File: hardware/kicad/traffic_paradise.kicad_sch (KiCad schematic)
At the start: 48 parts, among them J2 USB C, Q1 SS8050, Q2 SS8050, SW1 SW_Push, SW2 SW_Push, SW3 SW_Push, U1 ESP32-WROOM-32, U2 AMS1117-3.3, U3 USBLC6-2SC6, U4 CP2102N-A02-GQFN28

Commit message: Update KiCAD files
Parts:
- added R20, R21: 2k, Resistor_SMD:R_0402_1005Metric, symbol Device:R_Small_US
- D1: footprint Diode_SMD:D_0805_2012Metric -> Diode_SMD:D_SMA
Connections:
- net +3.3V: now also R20.1, R21.1
- net SCL: now also R20.2
- net SDA: now also R21.2

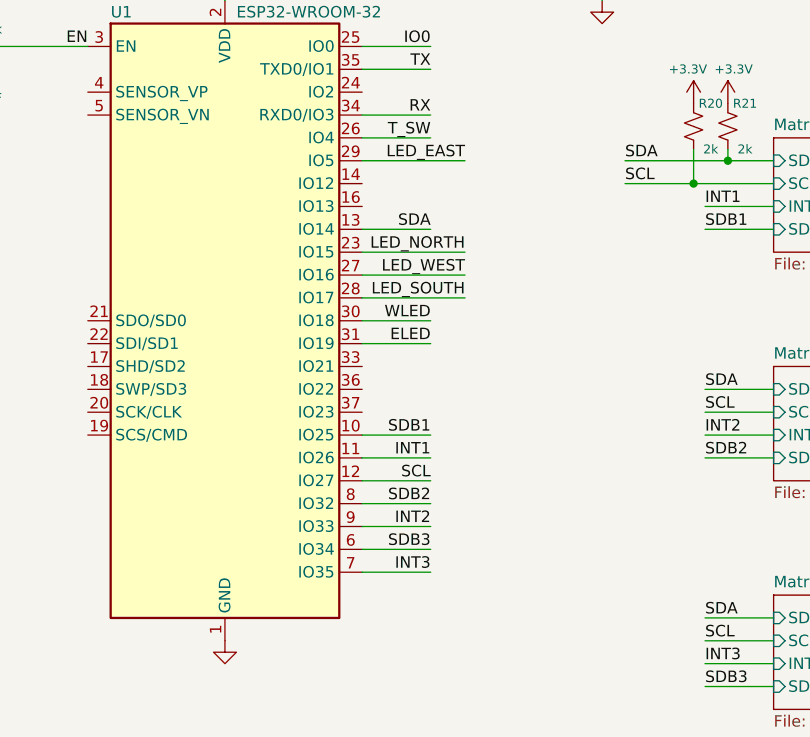
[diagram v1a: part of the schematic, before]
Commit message: move sbd/int lines off of input only gpio pins
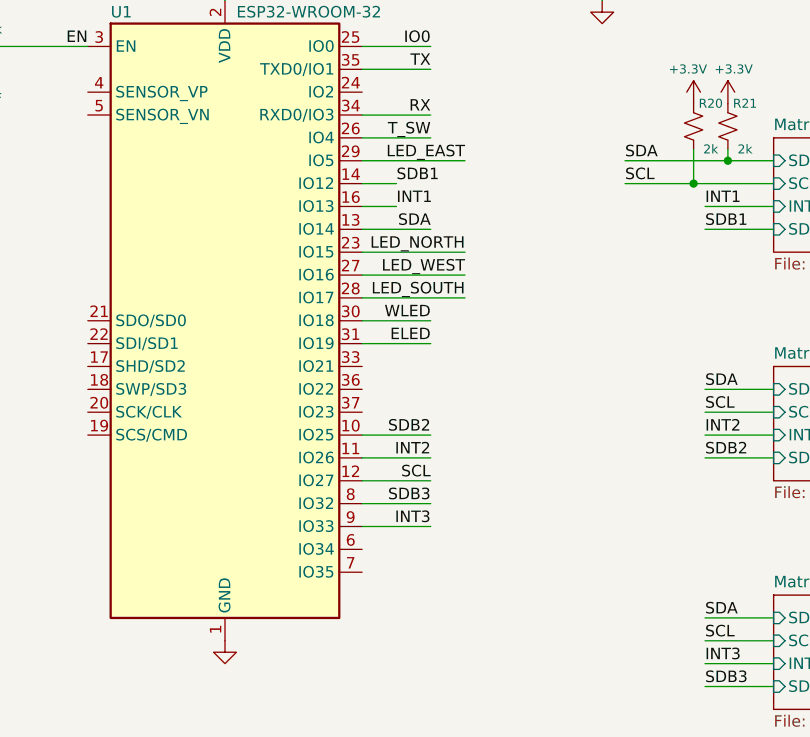
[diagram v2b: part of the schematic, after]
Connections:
- net INT1: now also U1.16 (IO13); no longer U1.11 (IO26)
- net INT2: now also U1.11 (IO26); no longer U1.9 (IO33)
- net INT3: now also U1.9 (IO33); no longer U1.7 (IO35)
- net SDB1: now also U1.14 (IO12); no longer U1.10 (IO25)
- net SDB2: now also U1.10 (IO25); no longer U1.8 (IO32)
- net SDB3: now also U1.8 (IO32); no longer U1.6 (IO34)

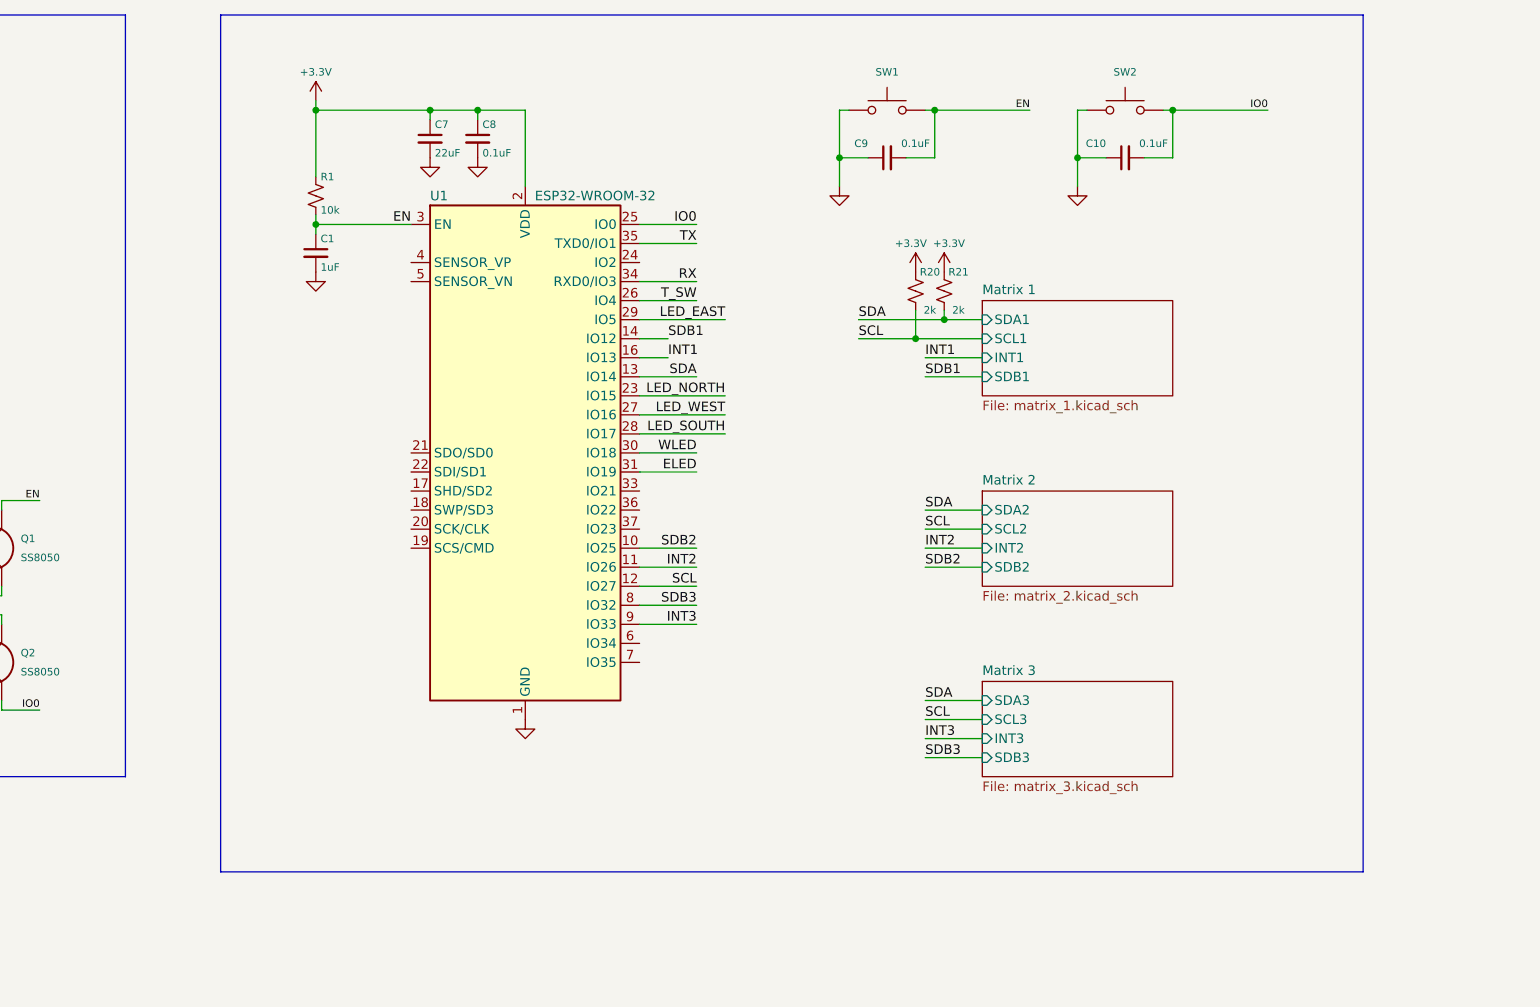
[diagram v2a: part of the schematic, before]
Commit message: move various esp32 pins to avoid strapping pins
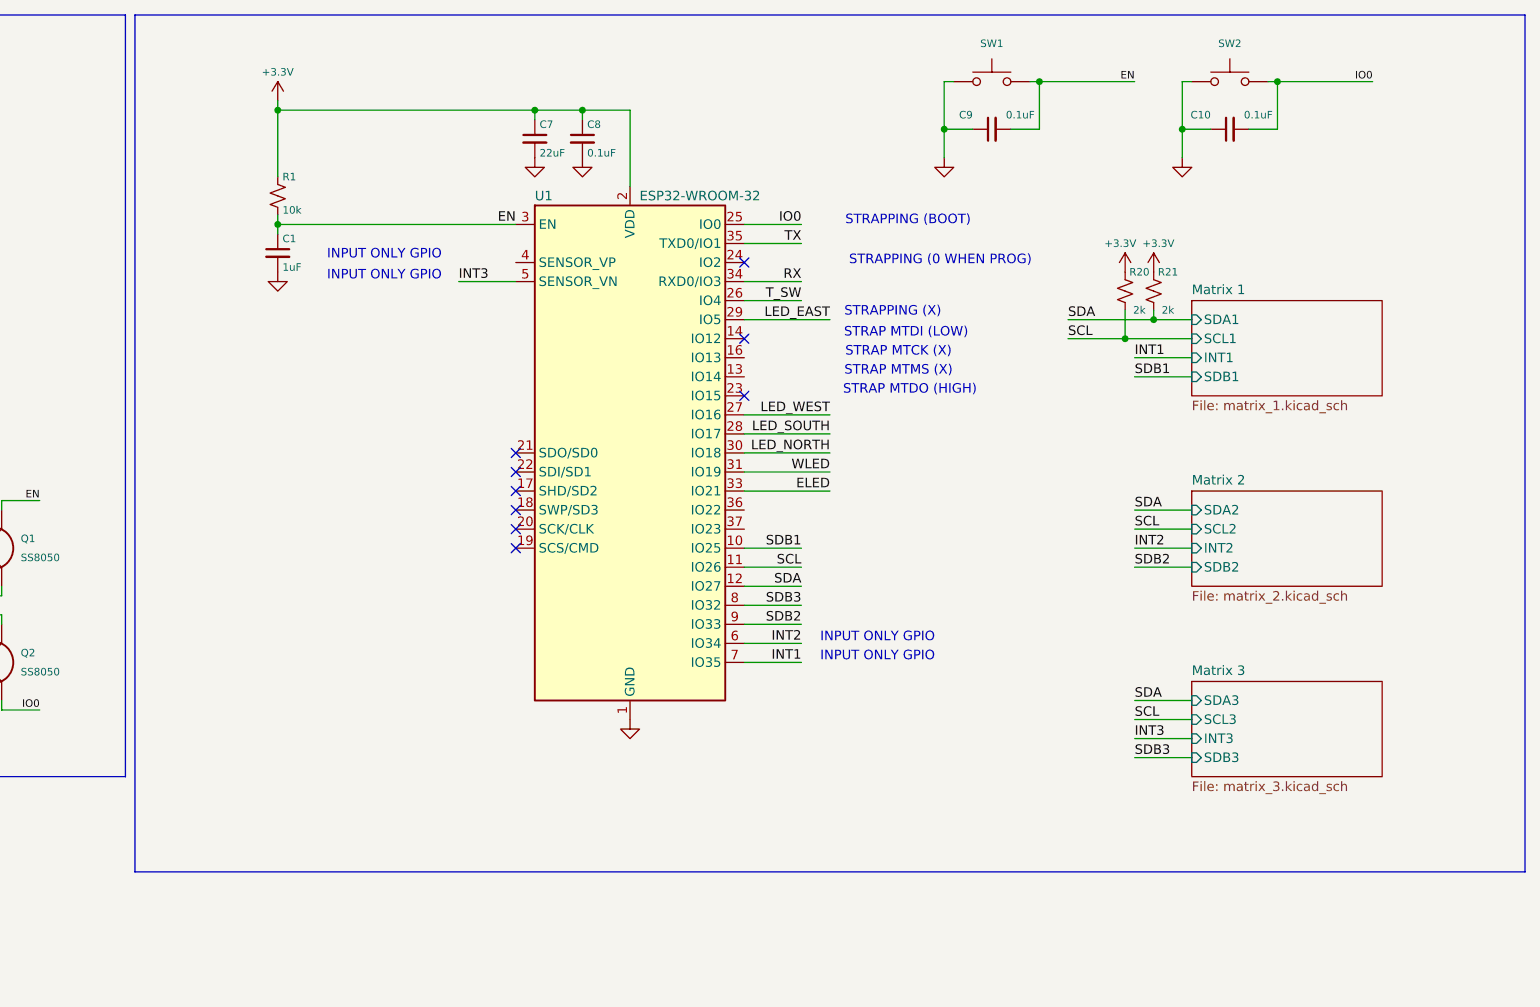
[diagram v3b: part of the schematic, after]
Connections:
- net ELED: now also U1.33 (IO21); no longer U1.31 (IO19)
- net INT1: now also U1.7 (IO35); no longer U1.16 (IO13)
- net INT2: now also U1.6 (IO34); no longer U1.11 (IO26)
- net INT3: now also U1.5 (SENSOR_VN); no longer U1.9 (IO33)
- net LED_NORTH: now also U1.30 (IO18); no longer U1.23 (IO15)
- net SCL: now also U1.11 (IO26); no longer U1.12 (IO27)
- net SDA: now also U1.12 (IO27); no longer U1.13 (IO14)
- net SDB1: now also U1.10 (IO25); no longer U1.14 (IO12)
- net SDB2: now also U1.9 (IO33); no longer U1.10 (IO25)
- net WLED: now also U1.31 (IO19); no longer U1.30 (IO18)
- no-connect marks 18 -> 27
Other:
- note added: "INPUT ONLY GPIO"
- note added: "STRAP MTCK (X)"
- note added: "STRAP MTDI (LOW)"
- note added: "STRAP MTDO (HIGH)"
- note added: "STRAP MTMS (X)"
- note added: "STRAPPING (0 WHEN PROG)"
- note added: "STRAPPING (BOOT)"
- note added: "STRAPPING (X)"
- moved on the sheet: C1, C10, C7, C8, C9, R1, R20, R21, SW1, SW2, U1

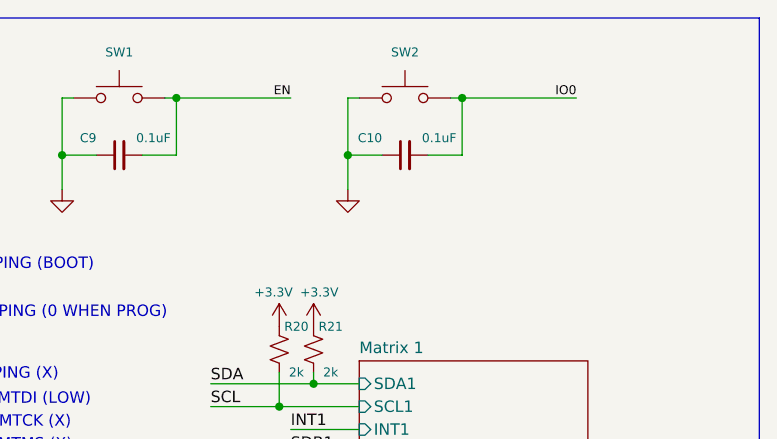
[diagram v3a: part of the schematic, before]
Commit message: Few changes
Added a missing power trace and removed C10 from assembly (can occasionally cause problems on resetting)
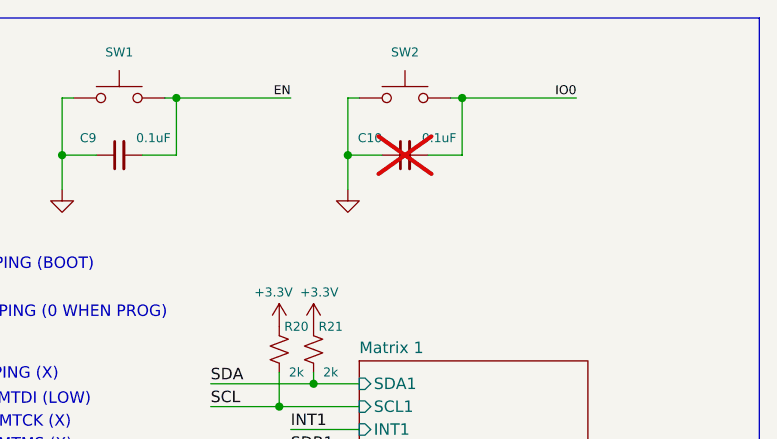
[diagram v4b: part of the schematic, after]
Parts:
- C10: now not fitted; now left out of the parts list
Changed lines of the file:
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@@
 		(unit 1)
 		(exclude_from_sim no)
-		(in_bom yes)
+		(in_bom no)
 		(on_board yes)
-		(dnp no)
+		(dnp yes)
 		(property "Reference" "C10"
 			(at 360.68 38.735 90)

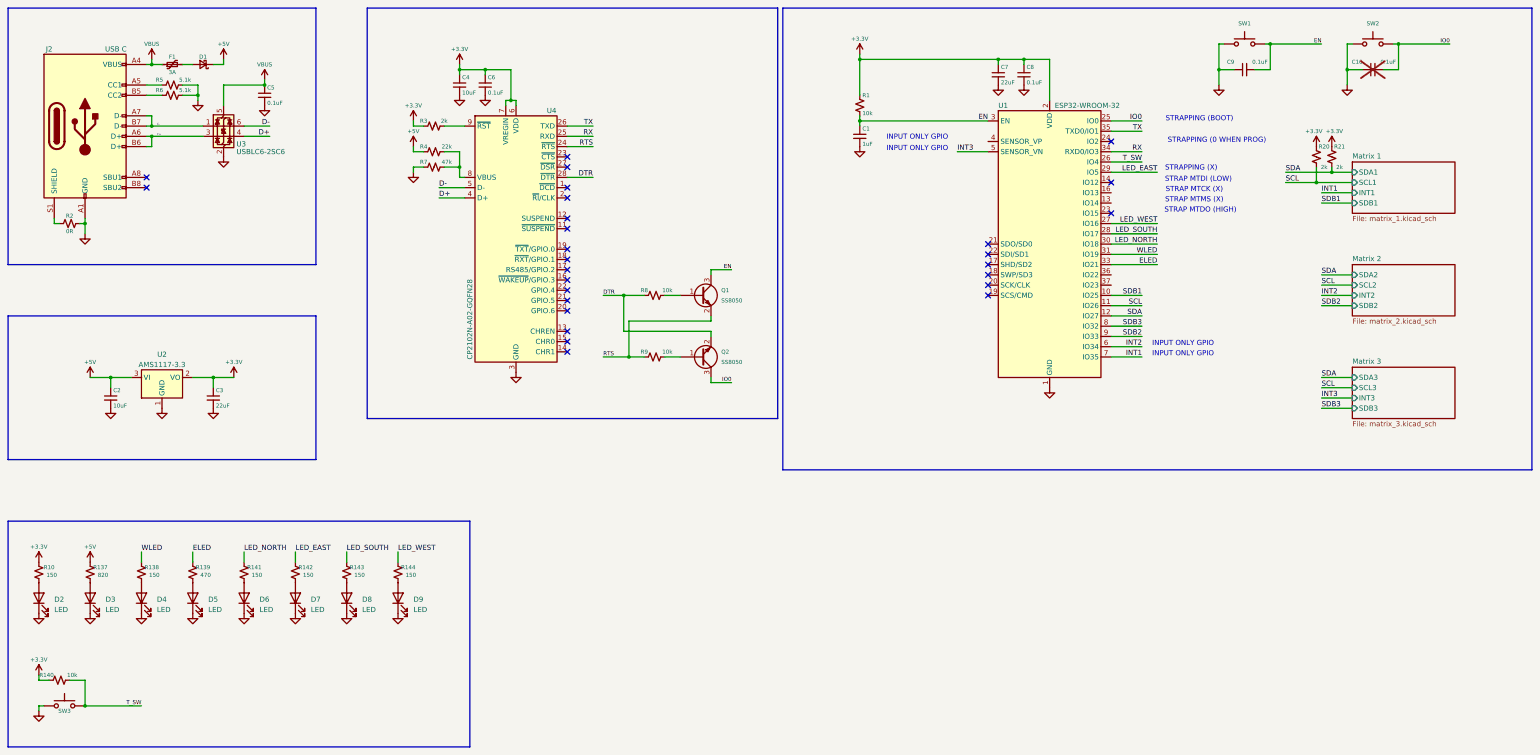
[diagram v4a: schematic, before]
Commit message: add I2C test points
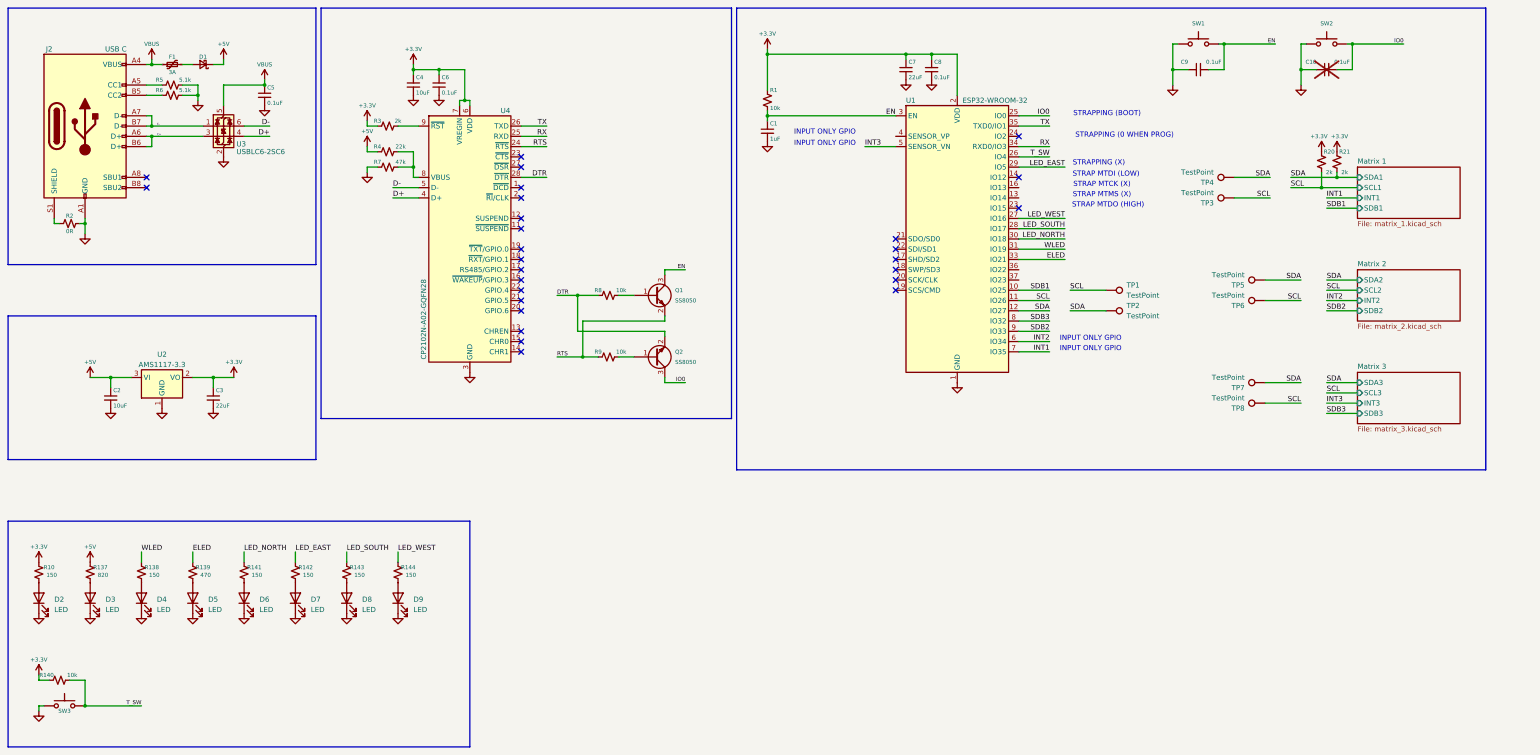
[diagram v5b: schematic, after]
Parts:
- added TP1, TP2, TP3, TP4, TP5, TP6, TP7, TP8: TestPoint, TestPoint:TestPoint_THTPad_1.5x1.5mm_Drill0.7mm, symbol Connector:TestPoint
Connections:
- net SCL: now also TP1.1, TP3.1, TP6.1, TP8.1
- net SDA: now also TP2.1, TP4.1, TP5.1, TP7.1
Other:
- moved on the sheet: C1, C10, C4, C6, C7, C8, C9, Q1, Q2, R1, R20, R21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

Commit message: fix uart lines
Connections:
- net RX: now also U4.26 (TXD); no longer U4.25 (RXD)
- net TX: now also U4.25 (RXD); no longer U4.26 (TXD)
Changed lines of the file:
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@@
 		)
 	)
-	(label "RX"
+	(label "TX"
 		(at 158.75 57.15 180)
 		(fields_autoplaced yes)
@@
 		)
 	)
-	(label "TX"
+	(label "RX"
 		(at 158.75 54.61 180)
 		(fields_autoplaced yes)

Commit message: move led_east to non-strapping pin
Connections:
- net LED_EAST: now also U1.36 (IO22); no longer U1.29 (IO5)
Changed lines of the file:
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@@
+	(wire
+		(pts
+			(xy 275.59 90.17) (xy 287.02 90.17)
+		)
+		(stroke
+			(width 0)
+			(type default)
+		)
+	)
 	(wire
 		(pts
@@
 		(pts
 			(xy 354.33 40.64) (xy 358.14 40.64)
-		)
-		(stroke
-			(width 0)
-			(type default)
-		)
-	)
-	(wire
-		(pts
-			(xy 275.59 64.77) (xy 287.02 64.77)
 		)
 		(stroke
@@
 		)
 	)
-	(label "LED_EAST"
-		(at 287.02 64.77 180)
-		(fields_autoplaced yes)
-		(effects
-			(font
-				(size 1.27 1.27)
-			)
-			(justify right bottom)
-		)
-	)
 	(label "SCL"
 		(at 283.21 97.79 180)
@@
 		(fields_autoplaced yes)
 		(effects
+			(font
+				(size 1.27 1.27)
+			)
+			(justify right bottom)
+		)
+	)
+	(label "LED_EAST"
+		(at 287.02 90.17 180)
+		(fields_autoplaced yes)
+		(effects
